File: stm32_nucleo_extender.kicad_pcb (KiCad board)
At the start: 2 copper layers, 103.8 x 162.9 mm, 6 parts, among them CN10 6-534206-9, CN7 6-534206-9, J1 TBL009-254-20GY-2GY, J2 TBL009-254-20GY-2GY, J3 TBL009-254-20GY-2GY, J4 TBL009-254-20GY-2GY

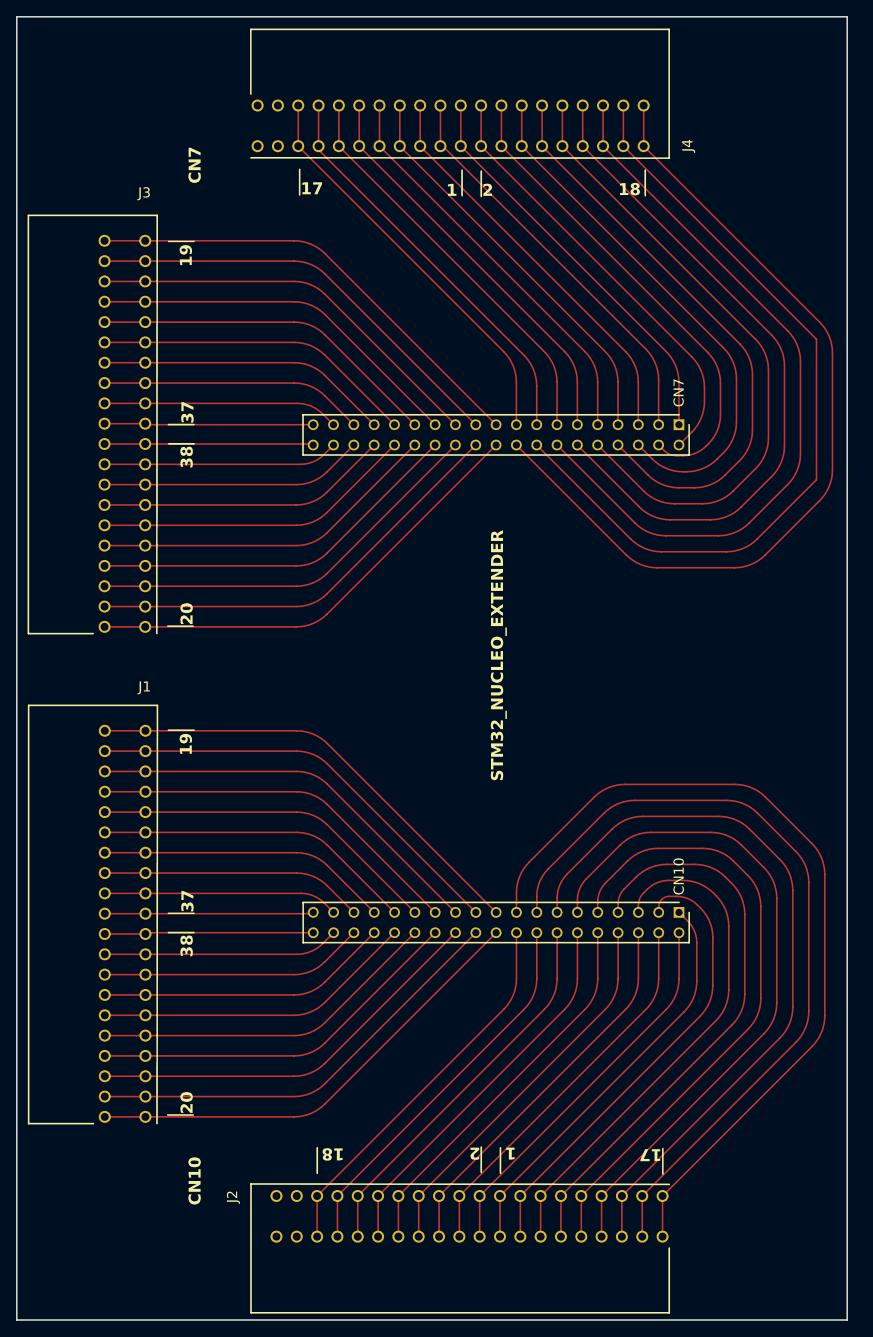
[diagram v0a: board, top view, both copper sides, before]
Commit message: [ADD] jlcpcb needed files
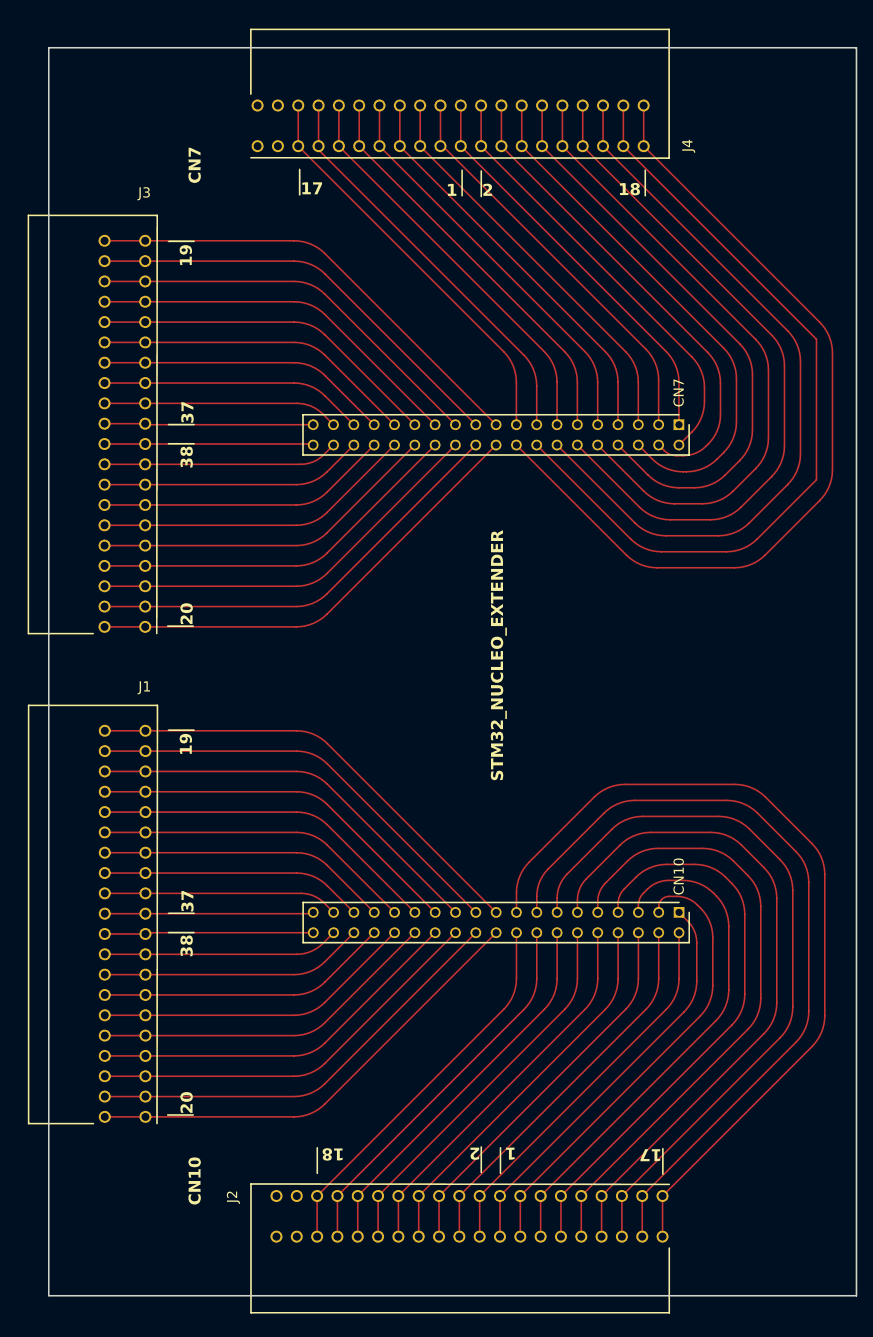
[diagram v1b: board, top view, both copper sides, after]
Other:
- board size 103.8 x 162.9 mm -> 101 x 156 mm
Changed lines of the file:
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@@
 		(capping no)
 		(filling no)
+		(aux_axis_origin 4.04 160)
+		(grid_origin 4.04 160)
 		(pcbplotparams
 			(layerselection 0x00000000_00000000_55555555_5755f5ff)
 			(plot_on_all_layers_selection 0x00000000_00000000_00000000_00000000)
 			(disableapertmacros no)
-			(usegerberextensions no)
+			(usegerberextensions yes)
 			(usegerberattributes yes)
 			(usegerberadvancedattributes yes)
-			(creategerberjobfile yes)
+			(creategerberjobfile no)
 			(dashed_line_dash_ratio 12)
 			(dashed_line_gap_ratio 3)
@@
 			(outputformat 1)
 			(mirror no)
-			(drillshape 1)
+			(drillshape 0)
 			(scaleselection 1)
-			(outputdirectory "")
+			(outputdirectory "Output/drill/")
 		)
 	)
@@
 	)
 	(gr_rect
-		(start 0.04 0.13)
-		(end 103.84 163.03)
+		(start 4.04 4)
+		(end 105 160)
 		(stroke
 			(width 0.2)

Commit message: [ADD] logo and holes
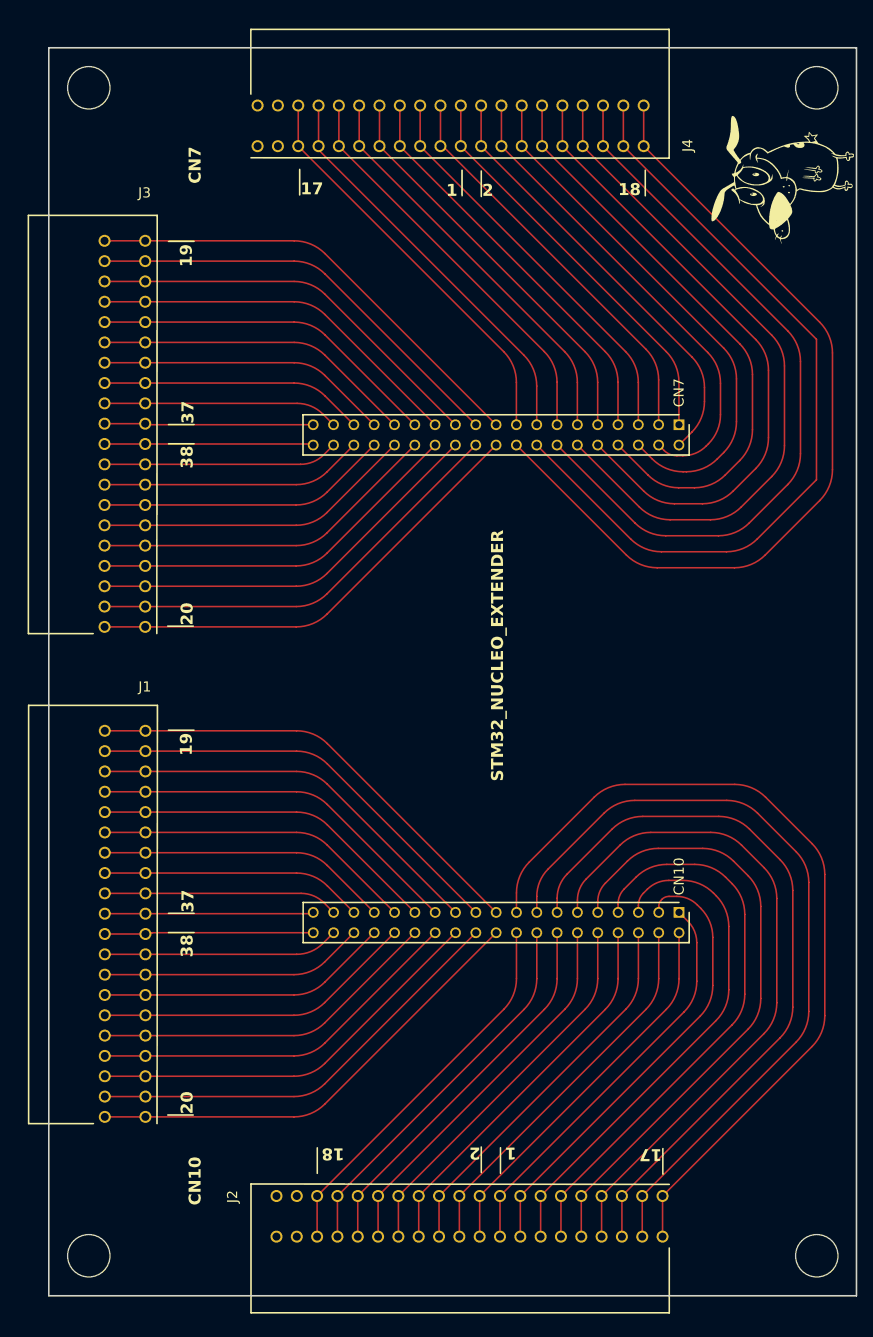
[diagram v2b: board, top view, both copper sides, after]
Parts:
- added G***: LOGO, logos:courage_logo, F.Cu at (95.8, 20.6)
- added REF**: MountingHole_5.3mm_M5_ISO14580, MountingHole:MountingHole_5.3mm_M5_ISO14580, F.Cu at (100.0, 9.00)
- added REF**: MountingHole_5.3mm_M5_ISO14580, MountingHole:MountingHole_5.3mm_M5_ISO14580, F.Cu at (100.0, 155.0)
- added REF**: MountingHole_5.3mm_M5_ISO14580, MountingHole:MountingHole_5.3mm_M5_ISO14580, F.Cu at (9.04, 9.00)
- added REF**: MountingHole_5.3mm_M5_ISO14580, MountingHole:MountingHole_5.3mm_M5_ISO14580, F.Cu at (9.04, 155.0)
